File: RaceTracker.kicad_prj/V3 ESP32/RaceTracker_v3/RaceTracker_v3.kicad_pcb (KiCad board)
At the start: 4 copper layers, 49 x 61 mm, 45 parts, among them J1 USB-C, J2 Battery, J3 Qwiic GPS (I2C), J4 microSD, J5 UART Debug, J6 e-Paper (steckbar) 8p, SW1 PWR, SW2 RESET, SW3 BOOT, U1 ESP32-S3-WROOM-1-N8, U2 MCP73831T-2ACI/OT, U3 AP2112K-3.3, U4 WSEN-ISDS

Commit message: V3: Kondensator-Abstaende zu ihren ICs verkleinert (<4mm)
Co-Authored-By: Claude Sonnet 5 <noreply@anthropic.com>
Claude-Session: https://claude.ai/code/session_01KJ1x8W8LsYuDo52VfB14br
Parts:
- moved J3 5.52 mm to (47.5, 76.5)
- moved C9 5.49 mm to (57.5, 53.0)
- moved R10 4.53 mm to (53.5, 77.0), turned to 180 degrees
- moved R11 4.53 mm to (53.5, 79.0), turned to 180 degrees
- moved SW1 3.54 mm to (54.7, 73.0)
- moved C4 3.44 mm to (48.0, 57.0)
- moved J4 3.00 mm to (86.0, 79.5)
- moved R14 2.55 mm to (89.0, 82.8)
- moved J6 2.35 mm to (57.8, 85.0)
- moved C10 1.72 mm to (57.5, 55.0)
- moved C7 1.68 mm to (57.5, 51.0)
- moved C6 1.48 mm to (78.8, 66.6)
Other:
- board size 49 x 61 mm -> 49 x 58.5 mm
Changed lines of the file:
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@@
 	(footprint "SW_DIP_SPSTx01_Slide_6.7x4.1mm_W7.62mm_P2.54mm_LowProfile"
 		(layer "F.Cu")
-		(at 54.195 76.5125)
+		(at 54.695 73.0125)
 		(descr "1x-dip-switch SPST , Slide, row spacing 7.62 mm (300 mils), body size 6.7x4.1mm (see e.g. https://www.ctscorp.com/wp-content/uploads/209-210.pdf), LowProfile")
 		(tags "DIP Switch SPST Slide 7.62mm 300mil LowProfile")
@@
 		)
 		(point
-			(at 58.005 76.5125)
+			(at 58.505 73.0125)
 			(size 1.27)
 			(layer "F.Fab")
@@
 	(footprint "microSD_HC_Molex_104031-0811"
 		(layer "F.Cu")
-		(at 86 82.5 90)
+		(at 86 79.5 90)
 		(descr "1.10mm Pitch microSD Memory Card Connector, Surface Mount, Push-Pull Type, 1.42mm Height, with Detect Switch (https://www.molex.com/pdm_docs/sd/1040310811_sd.pdf)")
 		(tags "microSD SD molex")
@@
 	(footprint "PinHeader_1x08_P2.54mm_Vertical"
 		(layer "F.Cu")
-		(at 56.61 87 90)
+		(at 57.84 85 90)
 		(descr "Through hole straight pin header, 1x08, 2.54mm pitch, single row")
 		(tags "Through hole pin header THT 1x08 2.54mm single row")
@@
 	(footprint "JST_SH_SM04B-SRSS-TB_1x04-1MP_P1.00mm_Horizontal"
 		(layer "F.Cu")
-		(at 48 82 -90)
+		(at 47.5 76.5 -90)
 		(descr "JST SH series connector, SM04B-SRSS-TB (http://www.jst-mfg.com/product/pdf/eng/eSH.pdf)")
 		(tags "connector JST SH horizontal")
@@
 	(footprint "R_0603_1608Metric"
 		(layer "B.Cu")
-		(at 52.95 83.5)
+		(at 53.5 79 180)
 		(descr "Resistor SMD 0603 (1608 Metric), square (rectangular) end terminal, IPC-7351 nominal, (Body size source: IPC-SM-782 page 72, https://www.pcb-3d.com/wordpress/wp-content/uploads/ipc-sm-782a_amendment_1_and_2.pdf)")
 		(tags "resistor")
@@
 		(duplicate_pad_numbers_are_jumpers no)
 		(fp_line
-			(start -0.237258 -0.5225)
-			(end 0.237258 -0.5225)
+			(start -0.237258 0.5225)
+			(end 0.237258 0.5225)
 			(stroke
 				(width 0.12)
@@
 		)
 		(fp_line
-			(start -0.237258 0.5225)
-			(end 0.237258 0.5225)
+			(start -0.237258 -0.5225)
+			(end 0.237258 -0.5225)
 			(stroke
 				(width 0.12)
@@
 		)
 		(pad "1" smd roundrect
-			(at -0.825 0)
+			(at -0.825 0 180)
 			(size 0.8 0.95)
 			(layers "B.Cu" "B.Mask" "B.Paste")
@@
 		)
 		(pad "2" smd roundrect
-			(at 0.825 0)
+			(at 0.825 0 180)
 			(size 0.8 0.95)
 			(layers "B.Cu" "B.Mask" "B.Paste")
@@
 	(footprint "C_0603_1608Metric"
 		(layer "B.Cu")
-		(at 56.5 56.4 180)
+		(at 57.5 55 180)
 		(descr "Capacitor SMD 0603 (1608 Metric), square (rectangular) end terminal, IPC-7351 nominal, (Body size source: IPC-SM-782 page 76, https://www.pcb-3d.com/wordpress/wp-content/uploads/ipc-sm-782a_amendment_1_and_2.pdf)")
 		(tags "capacitor")
@@
 	(footprint "C_0603_1608Metric"
 		(layer "B.Cu")
-		(at 48.5 60.4 -90)
+		(at 47.95 57 -90)
 		(descr "Capacitor SMD 0603 (1608 Metric), square (rectangular) end terminal, IPC-7351 nominal, (Body size source: IPC-SM-782 page 76, https://www.pcb-3d.com/wordpress/wp-content/uploads/ipc-sm-782a_amendment_1_and_2.pdf)")
 		(tags "capacitor")
@@
 	(footprint "C_0805_2012Metric"
 		(layer "B.Cu")
-		(at 56.5 52.35)
+		(at 57.5 51)
 		(descr "Capacitor SMD 0805 (2012 Metric), square (rectangular) end terminal, IPC-7351 nominal, (Body size source: IPC-SM-782 page 76, https://www.pcb-3d.com/wordpress/wp-content/uploads/ipc-sm-782a_amendment_1_and_2.pdf, https://docs.google.com/spreadsheets/d/1BsfQQcO9C6DZCsRaXUlFlo91Tg2WpOkGARC1WS5S8t0/edit?usp=sharing)")
 		(tags "capacitor")
@@
 	(footprint "R_0603_1608Metric"
 		(layer "B.Cu")
-		(at 88.5 85.325 -90)
+		(at 89 82.825 -90)
 		(descr "Resistor SMD 0603 (1608 Metric), square (rectangular) end terminal, IPC-7351 nominal, (Body size source: IPC-SM-782 page 72, https://www.pcb-3d.com/wordpress/wp-content/uploads/ipc-sm-782a_amendment_1_and_2.pdf)")
 		(tags "resistor")
@@
 	(footprint "R_0603_1608Metric"
 		(layer "B.Cu")
-		(at 52.95 81.5)
+		(at 53.5 77 180)
 		(descr "Resistor SMD 0603 (1608 Metric), square (rectangular) end terminal, IPC-7351 nominal, (Body size source: IPC-SM-782 page 72, https://www.pcb-3d.com/wordpress/wp-content/uploads/ipc-sm-782a_amendment_1_and_2.pdf)")
 		(tags "resistor")
@@
 		(duplicate_pad_numbers_are_jumpers no)
 		(fp_line
-			(start -0.237258 -0.5225)
-			(end 0.237258 -0.5225)
+			(start -0.237258 0.5225)
+			(end 0.237258 0.5225)
 			(stroke
 				(width 0.12)
@@
 		)
 		(fp_line
-			(start -0.237258 0.5225)
-			(end 0.237258 0.5225)
+			(start -0.237258 -0.5225)
+			(end 0.237258 -0.5225)
 			(stroke
 				(width 0.12)
@@
 		)
 		(pad "1" smd roundrect
-			(at -0.825 0)
+			(at -0.825 0 180)
 			(size 0.8 0.95)
 			(layers "B.Cu" "B.Mask" "B.Paste")
@@
 		)
 		(pad "2" smd roundrect
-			(at 0.825 0)
+			(at 0.825 0 180)
 			(size 0.8 0.95)
 			(layers "B.Cu" "B.Mask" "B.Paste")
@@
 	(footprint "C_0603_1608Metric"
 		(layer "B.Cu")
-		(at 56.5 58.4 180)
+		(at 57.5 53 180)
 		(descr "Capacitor SMD 0603 (1608 Metric), square (rectangular) end terminal, IPC-7351 nominal, (Body size source: IPC-SM-782 page 76, https://www.pcb-3d.com/wordpress/wp-content/uploads/ipc-sm-782a_amendment_1_and_2.pdf)")
 		(tags "capacitor")
@@
 	(footprint "C_0603_1608Metric"
 		(layer "B.Cu")
-		(at 80.275 66.775 180)
+		(at 78.8 66.629999 180)
 		(descr "Capacitor SMD 0603 (1608 Metric), square (rectangular) end terminal, IPC-7351 nominal, (Body size source: IPC-SM-782 page 76, https://www.pcb-3d.com/wordpress/wp-content/uploads/ipc-sm-782a_amendment_1_and_2.pdf)")
 		(tags "capacitor")
@@
 	(gr_rect
 		(start 43.95 28.5)
-		(end 93 89.5)
+		(end 93 87)
 		(stroke
 			(width 0.15)

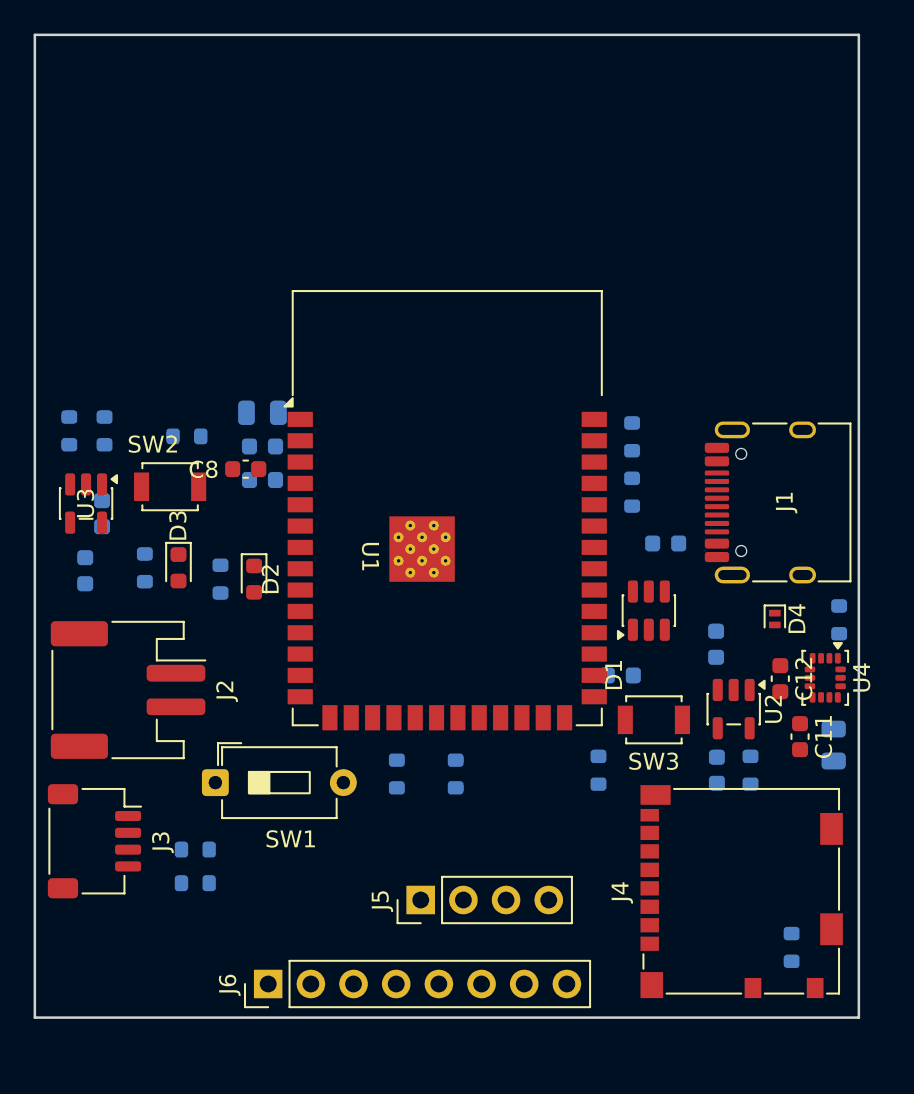
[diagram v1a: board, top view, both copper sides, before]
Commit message: V3: GND/+3V3-Ebenen + Power-Rails neu geroutet (Layer-Bug gefixt)
Co-Authored-By: Claude Sonnet 5 <noreply@anthropic.com>
Claude-Session: https://claude.ai/code/session_01KJ1x8W8LsYuDo52VfB14br
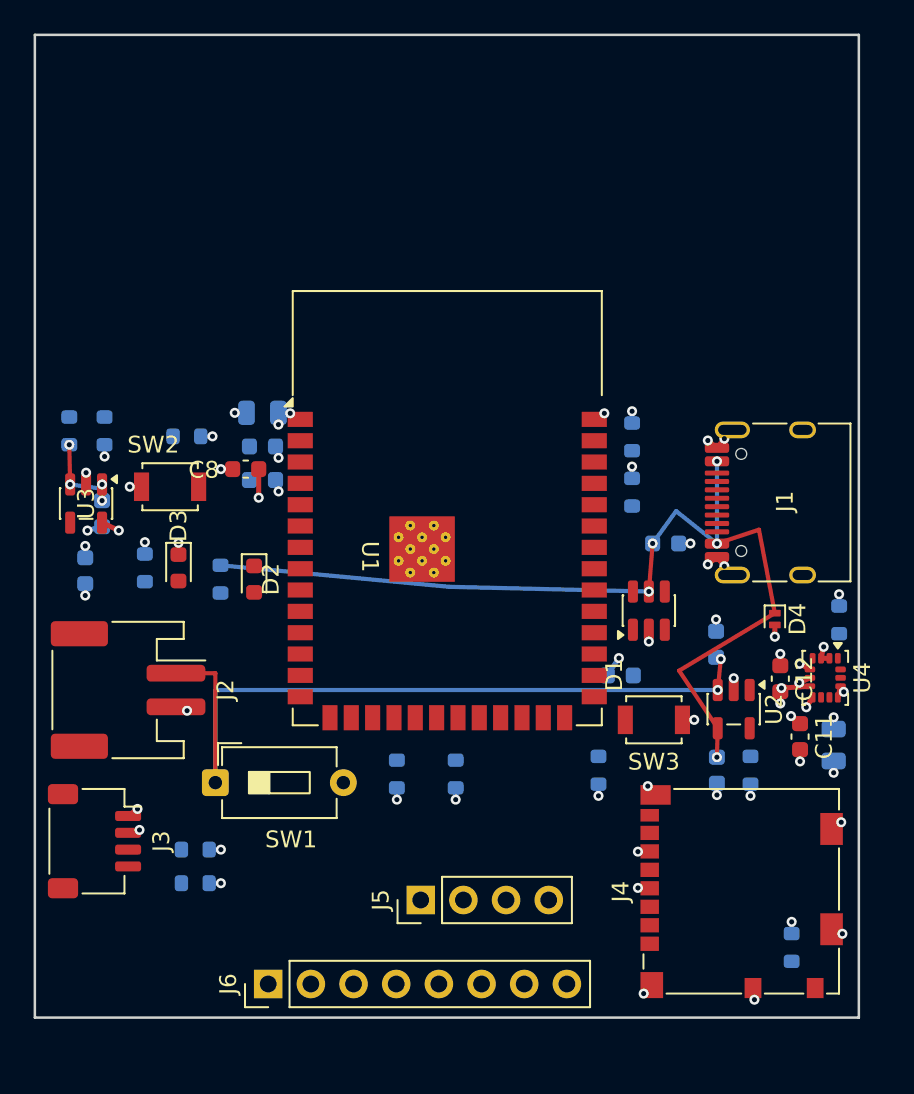
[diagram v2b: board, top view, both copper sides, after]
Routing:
- net /+VBUS: track 0.00 -> 59.0 mm, vias 0 -> 5
- net /+VBAT_RAW: track 0.00 -> 46.1 mm, vias 0 -> 2
- net /GND: track 0.00 -> 30.4 mm, vias 0 -> 41
- net /+3V3: track 0.00 -> 17.0 mm, vias 0 -> 21
- net /+VBAT_SYS: track 0.00 -> 5.52 mm, vias 0 -> 4
- added copper zone on In2.Cu, net /+3V3
- added copper zone on In1.Cu, net /GND

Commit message: V3: Signalnetze grossteils geroutet (10/25), DRC 0 echte Verstoesse
Co-Authored-By: Claude Sonnet 5 <noreply@anthropic.com>
Claude-Session: https://claude.ai/code/session_01KJ1x8W8LsYuDo52VfB14br
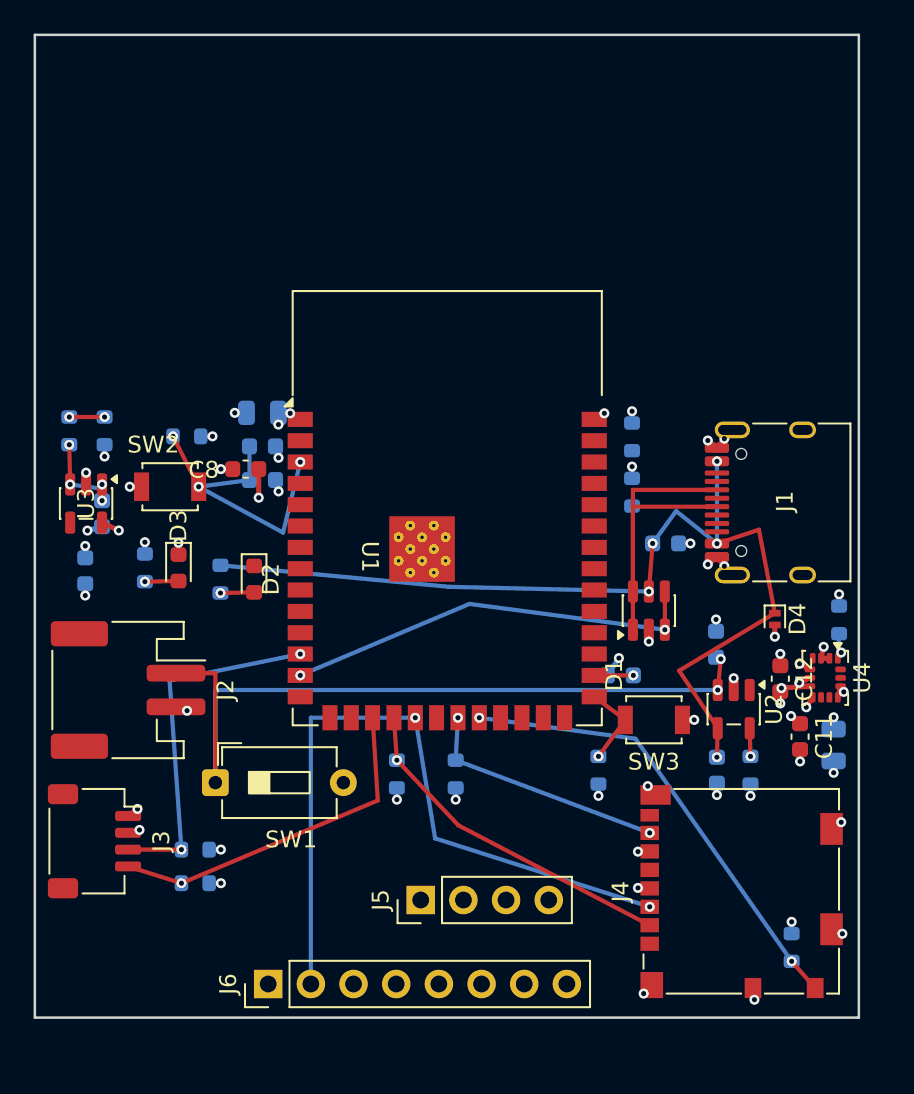
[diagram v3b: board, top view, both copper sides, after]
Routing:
- net /SD_MOSI: track 0.00 -> 42.7 mm, vias 0 -> 2
- net /SD_CD: track 0.00 -> 27.7 mm, vias 0 -> 2
- net /USB_DM: track 0.00 -> 24.9 mm, vias 0 -> 2
- net /USB_DP: track 0.00 -> 23.4 mm
- net /I2C_SDA: track 0.00 -> 21.2 mm, vias 0 -> 2
- net /I2C_SCL: track 0.00 -> 20.9 mm, vias 0 -> 1
- net /SD_CS: track 0.00 -> 20.7 mm, vias 0 -> 1
- net Net-(U1-EN): track 0.00 -> 18.5 mm, vias 0 -> 3
- net /SD_MISO: track 0.00 -> 14.9 mm, vias 0 -> 2
- net Net-(U1-IO0): track 0.00 -> 5.01 mm, vias 0 -> 1
- net /BATT_SENSE: track 0.00 -> 4.43 mm, vias 0 -> 3
- net /CHG_LED_A: track 0.00 -> 2.00 mm, vias 0 -> 1
- net /PWR_LED_A: track 0.00 -> 2.00 mm, vias 0 -> 1
- net /CHG_PROG: track 0.00 -> 1.68 mm, vias 0 -> 1
- net Net-(U4-SAO): track 0.00 -> 1.46 mm, vias 0 -> 1
